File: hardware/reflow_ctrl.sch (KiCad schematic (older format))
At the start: 36 parts, among them IC1 MAX6675, IC2 ATXMEGA128A4U-A, P1 PDI, U1 LT1129CST-3.3, U2 MOC3063, U3 BTA41/600B, X1 USB-Mini-B, X2 Mains, X3 Load, X4 Thermocouple

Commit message: Use big USB-B THT connector
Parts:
- X1: footprint uMIDI:USB-mini-B-UX60MB-5ST -> Connect:USB_B; symbol USB_OTG -> USB_B; Manufacturer (none) -> On Shore Technology Inc.; Manufacturer Part Number (none) -> USB-B1HSW6; Supplier (none) -> Digikey; Supplier Link (none) -> http://www.digikey.de/product-detail/de/USB-B1HSW6/ED2982-N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; Supplier Part Number (none) -> ED2982-ND
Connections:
- net labels added: USB_n, USB_p
- wire segments 90 -> 91
- no-connect marks 4 -> 3
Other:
- note added: "TODO\n* Complete supplier links\n* Add 3 Switches and approx. 3 LEDs\n* Select Heatsink\n* Add netclasses"
- note removed: "TODO\n* Complete supplier links\n* Add 3 Switches and approx. 3 LEDs\n* Replace USB connector by large type B (THT style)\n* Select Heatsink\n* Add netclasses"
- moved on the sheet: C1, C3, D1, D2, D3, R1
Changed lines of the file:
@@
 L TVS D1
 U 1 1 56AF2424
-P 1800 5400
-F 0 "D1" H 1800 5500 50  0000 C CNN
-F 1 "TVS 5V" H 1800 5300 50  0000 C CNN
-F 2 "Capacitors_SMD:C_0603" H 1800 5400 60  0001 C CNN
-F 3 "" H 1800 5400 60  0000 C CNN
-	1    1800 5400
+P 1550 5400
+F 0 "D1" H 1550 5500 50  0000 C CNN
+F 1 "TVS 5V" H 1550 5300 50  0000 C CNN
+F 2 "Capacitors_SMD:C_0603" H 1550 5400 60  0001 C CNN
+F 3 "" H 1550 5400 60  0000 C CNN
+	1    1550 5400
 	0    -1   -1   0
 $EndComp
@@
 L GND #PWR013
 U 1 1 56AF308D
-P 1800 5700
-F 0 "#PWR013" H 1800 5450 50  0001 C CNN
-F 1 "GND" H 1800 5550 50  0001 C CNN
-F 2 "" H 1800 5700 60  0000 C CNN
-F 3 "" H 1800 5700 60  0000 C CNN
-	1    1800 5700
+P 1550 5700
+F 0 "#PWR013" H 1550 5450 50  0001 C CNN
+F 1 "GND" H 1550 5550 50  0001 C CNN
+F 2 "" H 1550 5700 60  0000 C CNN
+F 3 "" H 1550 5700 60  0000 C CNN
+	1    1550 5700
 	1    0    0    -1
 $EndComp
@@
 L TVS D2
 U 1 1 56AF30D6
-P 2100 5400
-F 0 "D2" H 2100 5500 50  0000 C CNN
-F 1 "TVS 5V" H 2100 5300 50  0000 C CNN
-F 2 "Capacitors_SMD:C_0603" H 2100 5400 60  0001 C CNN
-F 3 "" H 2100 5400 60  0000 C CNN
-	1    2100 5400
+P 1850 5400
+F 0 "D2" H 1850 5500 50  0000 C CNN
+F 1 "TVS 5V" H 1850 5300 50  0000 C CNN
+F 2 "Capacitors_SMD:C_0603" H 1850 5400 60  0001 C CNN
+F 3 "" H 1850 5400 60  0000 C CNN
+	1    1850 5400
 	0    -1   -1   0
 $EndComp
@@
 L GND #PWR014
 U 1 1 56AF30DC
-P 2100 5700
-F 0 "#PWR014" H 2100 5450 50  0001 C CNN
-F 1 "GND" H 2100 5550 50  0001 C CNN
-F 2 "" H 2100 5700 60  0000 C CNN
-F 3 "" H 2100 5700 60  0000 C CNN
-	1    2100 5700
+P 1850 5700
+F 0 "#PWR014" H 1850 5450 50  0001 C CNN
+F 1 "GND" H 1850 5550 50  0001 C CNN
+F 2 "" H 1850 5700 60  0000 C CNN
+F 3 "" H 1850 5700 60  0000 C CNN
+	1    1850 5700
 	1    0    0    -1
 $EndComp
@@
 L TVS D3
 U 1 1 56AF3111
-P 2400 5400
-F 0 "D3" H 2400 5500 50  0000 C CNN
-F 1 "TVS 5V" H 2400 5300 50  0000 C CNN
-F 2 "Capacitors_SMD:C_0603" H 2400 5400 60  0001 C CNN
-F 3 "" H 2400 5400 60  0000 C CNN
-	1    2400 5400
+P 2150 5400
+F 0 "D3" H 2150 5500 50  0000 C CNN
+F 1 "TVS 5V" H 2150 5300 50  0000 C CNN
+F 2 "Capacitors_SMD:C_0603" H 2150 5400 60  0001 C CNN
+F 3 "" H 2150 5400 60  0000 C CNN
+	1    2150 5400
 	0    -1   -1   0
 $EndComp
@@
 L GND #PWR015
 U 1 1 56AF3117
-P 2400 5700
-F 0 "#PWR015" H 2400 5450 50  0001 C CNN
-F 1 "GND" H 2400 5550 50  0001 C CNN
-F 2 "" H 2400 5700 60  0000 C CNN
-F 3 "" H 2400 5700 60  0000 C CNN
-	1    2400 5700
-	1    0    0    -1
-$EndComp
-$Comp
-L USB_OTG X1
+P 2150 5700
+F 0 "#PWR015" H 2150 5450 50  0001 C CNN
+F 1 "GND" H 2150 5550 50  0001 C CNN
+F 2 "" H 2150 5700 60  0000 C CNN
+F 3 "" H 2150 5700 60  0000 C CNN
+	1    2150 5700
+	1    0    0    -1
+$EndComp
+$Comp
+L USB_B X1
 U 1 1 56AF3747
-P 1400 4800
-F 0 "X1" V 1100 4900 50  0000 C CNN
-F 1 "USB-Mini-B" H 1400 5000 50  0000 C CNN
-F 2 "uMIDI:USB-mini-B-UX60MB-5ST" V 1350 4700 60  0001 C CNN
-F 3 "" V 1350 4700 60  0000 C CNN
-	1    1400 4800
+P 1150 4800
+F 0 "X1" V 850 4900 50  0000 C CNN
+F 1 "USB-Mini-B" H 1150 5000 50  0000 C CNN
+F 2 "Connect:USB_B" V 1100 4700 60  0001 C CNN
+F 3 "http://www.on-shore.com/sites/default/files/manuals/usb-b1hsxx.pdf" V 1100 4700 60  0001 C CNN
+F 4 "ED2982-ND" V 850 4900 50  0001 C CNN "Supplier Part Number"
+F 5 "http://www.digikey.de/product-detail/de/USB-B1HSW6/ED2982-ND/2677743" V 850 4900 50  0001 C CNN "Supplier Link"
+F 6 "On Shore Technology Inc." V 850 4900 50  0001 C CNN "Manufacturer"
+F 7 "Digikey" V 850 4900 50  0001 C CNN "Supplier"
+F 8 "USB-B1HSW6" V 850 4900 50  0001 C CNN "Manufacturer Part Number"
+	1    1150 4800
 	0    -1   1    0
 $EndComp
-Text GLabel 1750 4550 1    60   Input ~ 0
+Text GLabel 1500 4550 1    60   Input ~ 0
 VBUS
 $Comp
 L GND #PWR016
 U 1 1 56AF578E
-P 1700 5000
-F 0 "#PWR016" H 1700 4750 50  0001 C CNN
-F 1 "GND" H 1700 4850 50  0001 C CNN
-F 2 "" H 1700 5000 60  0000 C CNN
-F 3 "" H 1700 5000 60  0000 C CNN
-	1    1700 5000
-	1    0    0    -1
-$EndComp
-NoConn ~ 1700 4900
+P 1450 4950
+F 0 "#PWR016" H 1450 4700 50  0001 C CNN
+F 1 "GND" H 1450 4800 50  0001 C CNN
+F 2 "" H 1450 4950 60  0000 C CNN
+F 3 "" H 1450 4950 60  0000 C CNN
+	1    1450 4950
+	1    0    0    -1
+$EndComp
 $Comp
 L C C1
 U 1 1 56AF63F3
-P 1200 5450
-F 0 "C1" H 1050 5550 50  0000 L CNN
-F 1 "4.7n" H 1000 5350 50  0000 L CNN
-F 2 "Capacitors_SMD:C_0603" H 1238 5300 30  0001 C CNN
-F 3 "" H 1200 5450 60  0000 C CNN
-	1    1200 5450
+P 950 5400
+F 0 "C1" H 800 5500 50  0000 L CNN
+F 1 "4.7n" H 750 5300 50  0000 L CNN
+F 2 "Capacitors_SMD:C_0603" H 988 5250 30  0001 C CNN
+F 3 "" H 950 5400 60  0000 C CNN
+	1    950  5400
 	1    0    0    -1
 $EndComp
@@
 L R R1
 U 1 1 56AF6523
-P 1400 5450
-F 0 "R1" V 1500 5450 50  0000 C CNN
-F 1 "1M" V 1400 5450 50  0000 C CNN
-F 2 "Resistors_SMD:R_0603" V 1330 5450 30  0001 C CNN
-F 3 "" H 1400 5450 30  0000 C CNN
-	1    1400 5450
+P 1150 5400
+F 0 "R1" V 1250 5400 50  0000 C CNN
+F 1 "1M" V 1150 5400 50  0000 C CNN
+F 2 "Resistors_SMD:R_0603" V 1080 5400 30  0001 C CNN
+F 3 "" H 1150 5400 30  0000 C CNN
+	1    1150 5400
 	1    0    0    -1
 $EndComp
@@
 L GND #PWR017
 U 1 1 56AF75D9
-P 1300 5700
-F 0 "#PWR017" H 1300 5450 50  0001 C CNN
-F 1 "GND" H 1300 5550 50  0001 C CNN
-F 2 "" H 1300 5700 60  0000 C CNN
-F 3 "" H 1300 5700 60  0000 C CNN
-	1    1300 5700
+P 1050 5650
+F 0 "#PWR017" H 1050 5400 50  0001 C CNN
+F 1 "GND" H 1050 5500 50  0001 C CNN
+F 2 "" H 1050 5650 60  0000 C CNN
+F 3 "" H 1050 5650 60  0000 C CNN
+	1    1050 5650
 	1    0    0    -1
 $EndComp
@@
 L C C3
 U 1 1 56AF8768
-P 2000 4600
-F 0 "C3" V 1950 4650 50  0000 L CNN
-F 1 "100n" V 2050 4650 50  0000 L CNN
-F 2 "Capacitors_SMD:C_0603" H 2038 4450 30  0001 C CNN
-F 3 "" H 2000 4600 60  0001 C CNN
-	1    2000 4600
+P 1750 4600
+F 0 "C3" V 1700 4650 50  0000 L CNN
+F 1 "100n" V 1800 4650 50  0000 L CNN
+F 2 "Capacitors_SMD:C_0603" H 1788 4450 30  0001 C CNN
+F 3 "" H 1750 4600 60  0001 C CNN
+	1    1750 4600
 	0    1    1    0
 $EndComp
@@
 L GND #PWR018
 U 1 1 56AF8D20
-P 2250 4600
-F 0 "#PWR018" H 2250 4350 50  0001 C CNN
-F 1 "GND" H 2250 4450 50  0001 C CNN
-F 2 "" H 2250 4600 60  0000 C CNN
-F 3 "" H 2250 4600 60  0000 C CNN
-	1    2250 4600
+P 2000 4600
+F 0 "#PWR018" H 2000 4350 50  0001 C CNN
+F 1 "GND" H 2000 4450 50  0001 C CNN
+F 2 "" H 2000 4600 60  0000 C CNN
+F 3 "" H 2000 4600 60  0000 C CNN
+	1    2000 4600
 	0    -1   -1   0
 $EndComp
@@
 Connection ~ 2150 2650
 Wire Wire Line
-	1700 4600 1850 4600
-Wire Wire Line
-	1750 4600 1750 4550
-Wire Wire Line
-	1800 4600 1800 5100
-Connection ~ 1750 4600
-Wire Wire Line
-	1700 4700 2600 4700
-Wire Wire Line
-	2400 4700 2400 5100
-Wire Wire Line
-	1700 4800 2600 4800
-Wire Wire Line
-	2100 4800 2100 5100
-Connection ~ 2100 4800
-Connection ~ 2400 4700
-Wire Wire Line
-	1300 5200 1300 5250
-Connection ~ 1300 5250
-Wire Wire Line
-	1400 5650 1400 5600
-Wire Wire Line
-	1200 5650 1200 5600
-Wire Wire Line
-	1300 5700 1300 5650
-Wire Wire Line
-	1200 5650 1400 5650
-Connection ~ 1300 5650
-Wire Wire Line
-	1200 5300 1200 5250
-Wire Wire Line
-	1200 5250 1400 5250
-Wire Wire Line
-	1400 5250 1400 5300
-Connection ~ 1800 4600
-Wire Wire Line
-	2150 4600 2250 4600
+	1450 4600 1600 4600
+Wire Wire Line
+	1500 4600 1500 4550
+Wire Wire Line
+	1550 4600 1550 5100
+Connection ~ 1500 4600
+Wire Wire Line
+	1450 4700 2600 4700
+Wire Wire Line
+	2150 4700 2150 5100
+Wire Wire Line
+	1450 4800 2600 4800
+Wire Wire Line
+	1850 4800 1850 5100
+Connection ~ 1850 4800
+Connection ~ 2150 4700
+Wire Wire Line
+	1050 5100 1050 5200
+Connection ~ 1050 5200
+Wire Wire Line
+	1150 5600 1150 5550
+Wire Wire Line
+	950  5600 950  5550
+Wire Wire Line
+	1050 5650 1050 5600
+Wire Wire Line
+	950  5600 1150 5600
+Connection ~ 1050 5600
+Wire Wire Line
+	950  5250 950  5200
+Wire Wire Line
+	950  5200 1150 5200
+Wire Wire Line
+	1150 5200 1150 5250
+Connection ~ 1550 4600
+Wire Wire Line
+	1900 4600 2000 4600
 Wire Wire Line
 	1550 7100 1750 7100
@@
 $EndComp
 Text Notes 4000 6750 0    60   ~ 0
-TODO\n* Complete supplier links\n* Add 3 Switches and approx. 3 LEDs\n* Replace USB connector by large type B (THT style)\n* Select Heatsink\n* Add netclasses
+TODO\n* Complete supplier links\n* Add 3 Switches and approx. 3 LEDs\n* Select Heatsink\n* Add netclasses
+Wire Wire Line
+	1450 4950 1450 4900
+Text Label 2250 4700 0    60   ~ 0
+USB_p
+Text Label 2250 4800 0    60   ~ 0
+USB_n
 $EndSCHEMATC

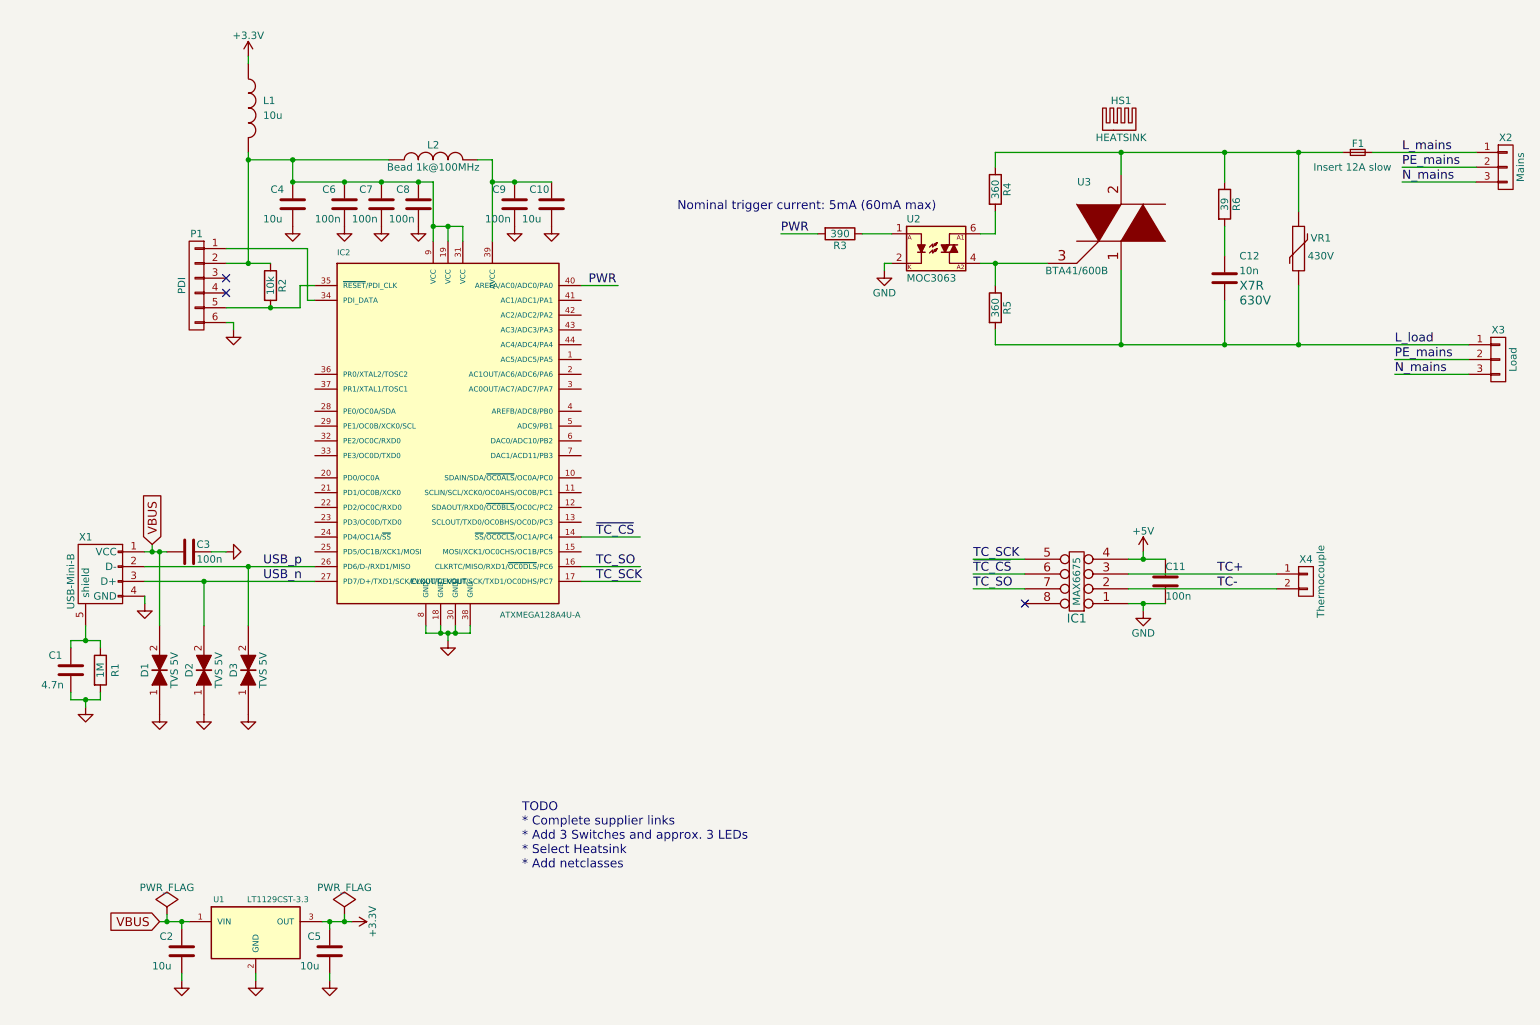
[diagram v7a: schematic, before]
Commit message: Remove MCU circuit (use external uMIDI)
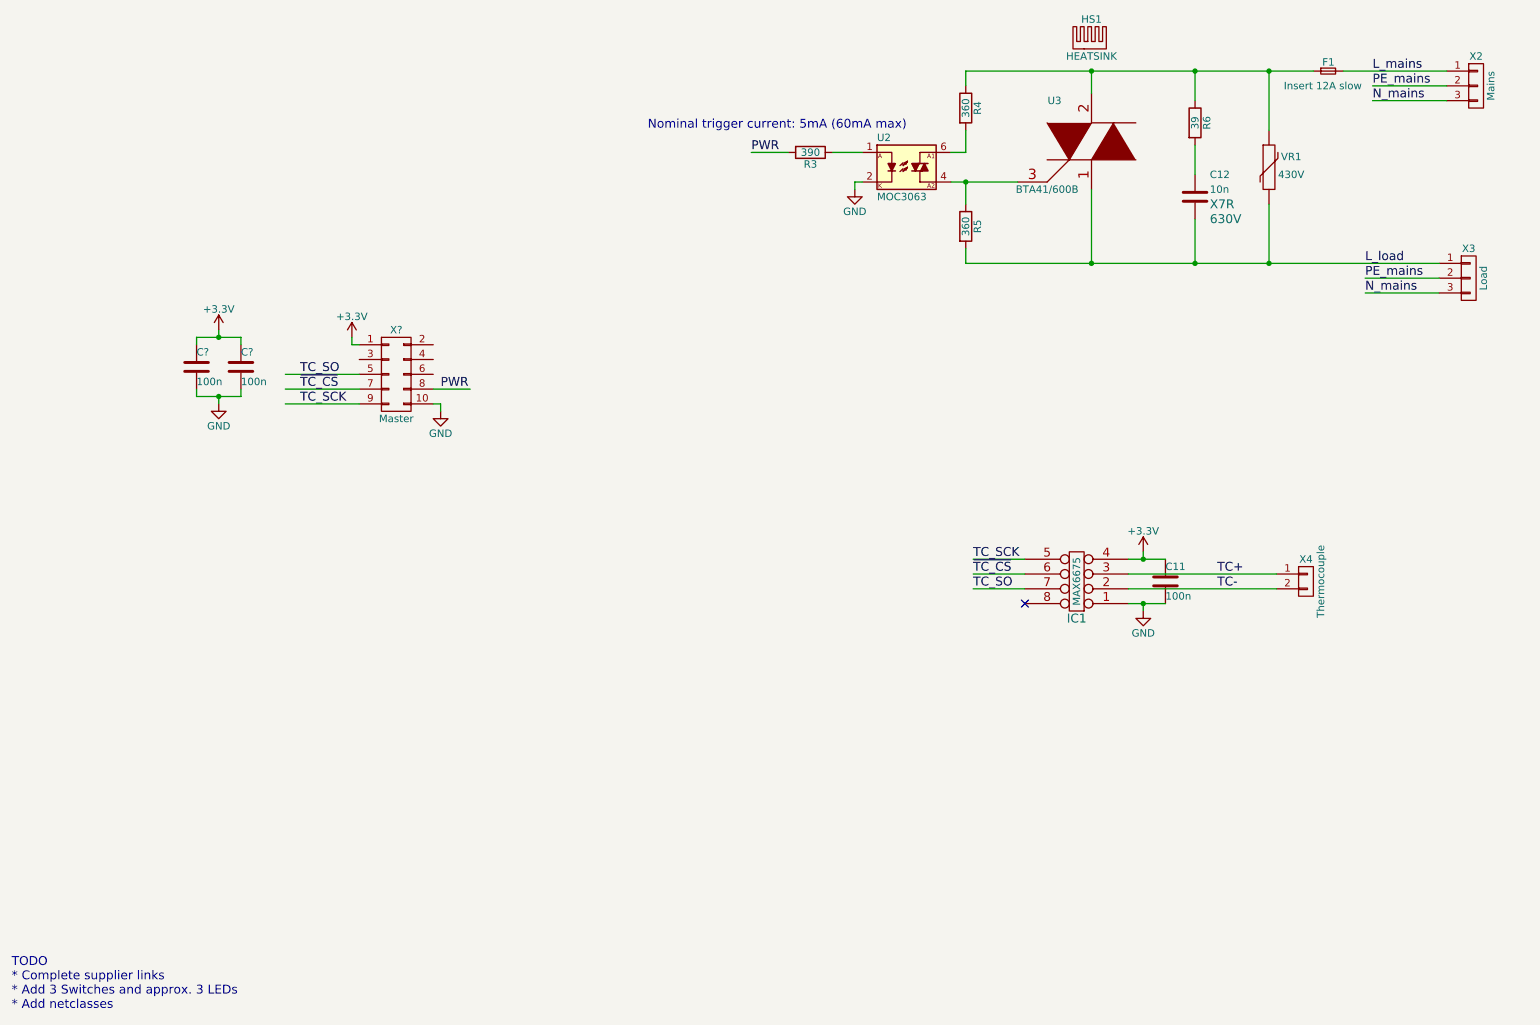
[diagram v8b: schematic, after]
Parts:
- removed C1: 4.7n, Capacitors_SMD:C_0603, symbol C
- removed C10, C2, C4, C5: 10u, Capacitors_SMD:C_0603, symbol C
- removed C3, C6, C7, C8, C9: 100n, Capacitors_SMD:C_0603, symbol C
- removed D1, D2, D3: TVS 5V, Capacitors_SMD:C_0603, symbol TVS
- removed IC2: ATXMEGA128A4U-A, Housings_QFP:TQFP-44_10x10mm_Pitch0.8mm, symbol ATXMEGA128A4U-A
- removed L1: 10u, Capacitors_SMD:C_0603, symbol INDUCTOR
- removed L2: Bead 1k@100MHz, Capacitors_SMD:C_0603, symbol INDUCTOR
- removed P1: PDI, Pin_Headers:Pin_Header_Straight_2x03, symbol CONN_01X06
- removed R1: 1M, Resistors_SMD:R_0603, symbol R
- removed R2: 10k, Resistors_SMD:R_0603, symbol R
- removed U1: LT1129CST-3.3, uMIDI:SOT-223, symbol LT1129CST-3.3
- removed X1: USB-Mini-B, Connect:USB_B, symbol USB_B
- added C? (x2): 100n, Capacitors_SMD:C_0603, symbol C
- added X?: Master, symbol CONN_02X05
- HS1: Manufacturer (none) -> Fischer Elektronik; Manufacturer Part Number (none) -> SK 129-50 STS; Supplier (none) -> Reichelt
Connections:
- net labels removed: +5V, USB_n, USB_p, VBUS
- wire segments 91 -> 49
- no-connect marks 3 -> 1
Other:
- note added: "TODO\n* Complete supplier links\n* Add 3 Switches and approx. 3 LEDs\n* Add netclasses"
- note removed: "TODO\n* Complete supplier links\n* Add 3 Switches and approx. 3 LEDs\n* Select Heatsink\n* Add netclasses"
- moved on the sheet: C12, F1, HS1, R3, R4, R5, R6, U2, U3, VR1, X2, X3
